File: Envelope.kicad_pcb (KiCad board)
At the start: 2 copper layers, 39.5 x 100 mm, 81 parts, among them J1 Conn_02x05_Odd_Even, J2 Conn_02x03_Odd_Even, J3 Conn_01x06, SW1 SW_SPDT_MSM, SW2 SW_SPDT_MSM, SW3 SW_Push, U1 TL072, U2 ATmega328PB-AU, U3 L7805, Y1 20MHz

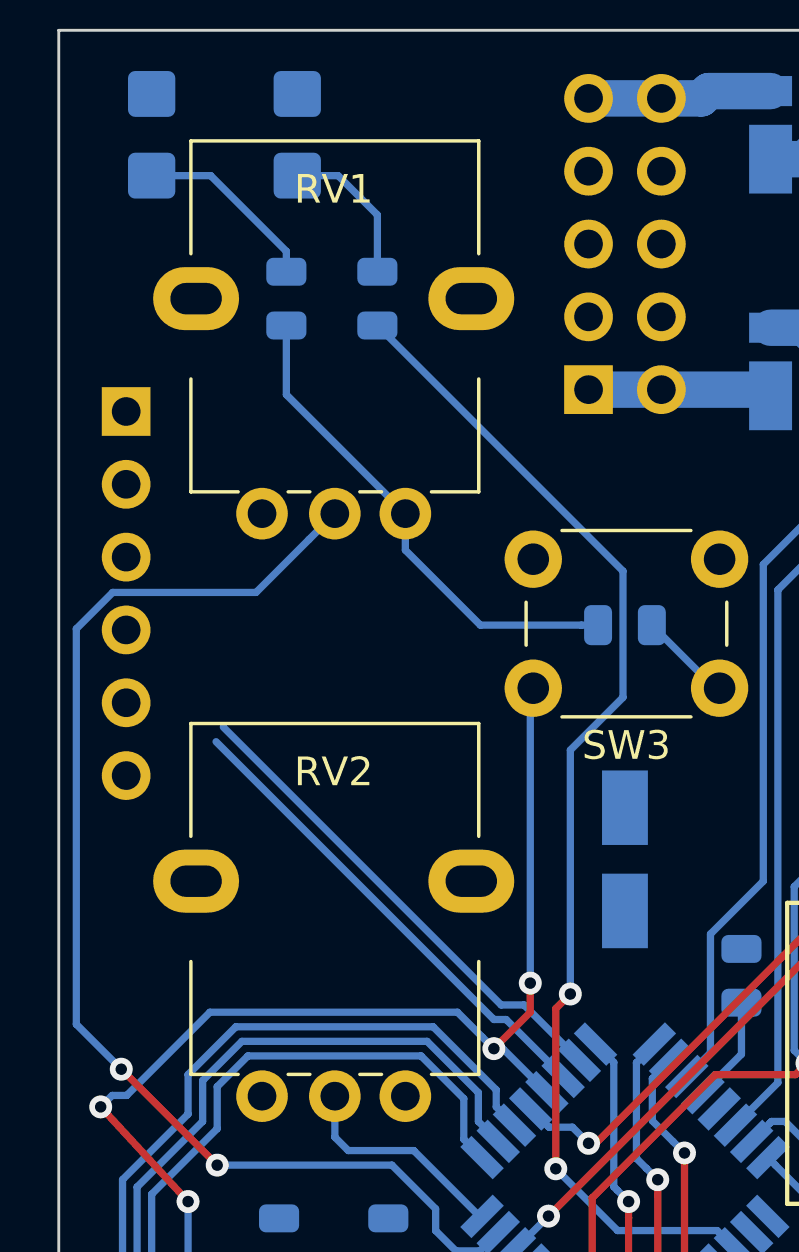
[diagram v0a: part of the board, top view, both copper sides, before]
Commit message: Use 3-pin connector for serial.
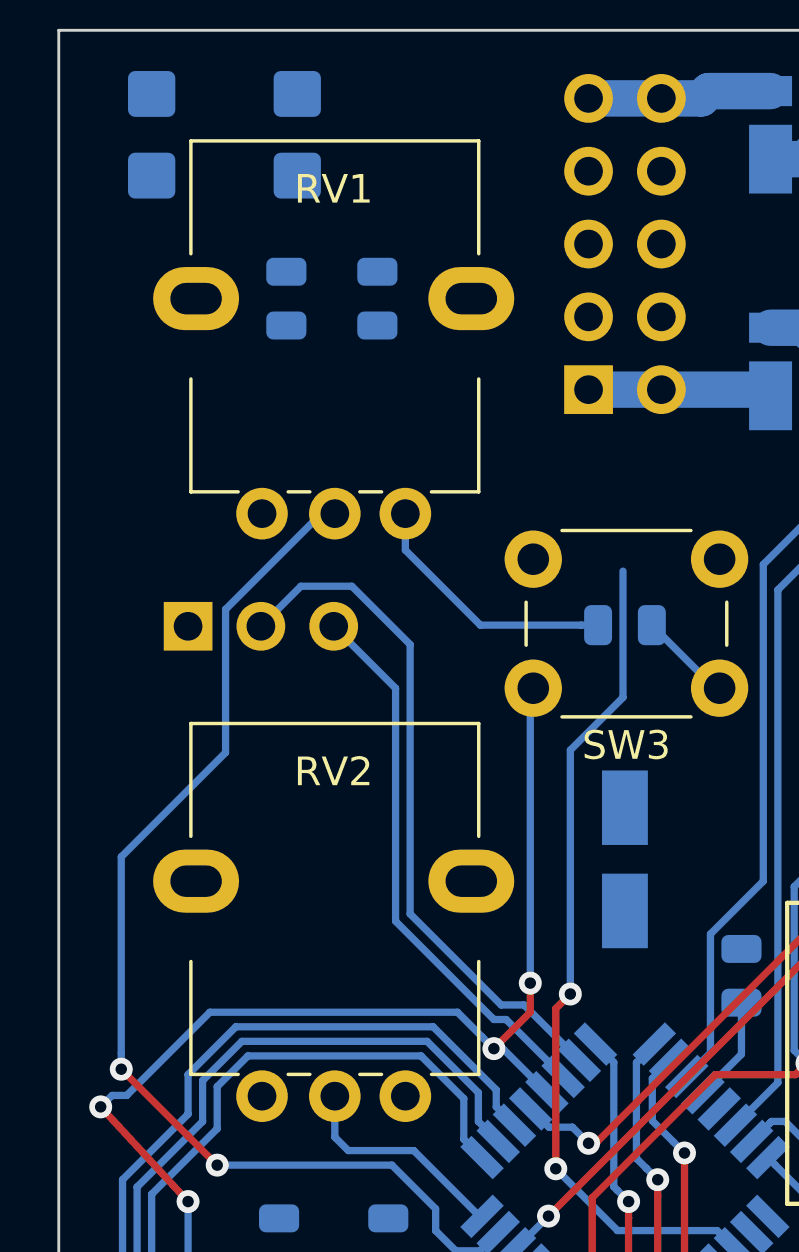
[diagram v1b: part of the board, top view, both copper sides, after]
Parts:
- J3: value Conn_01x06 -> Conn_01x03; footprint Connector_PinHeader_2.54mm:PinHeader_1x06_P2.54mm_Vertical -> Connector_PinHeader_2.54mm:PinHeader_1x03_P2.54mm_Vertical
- moved J3 7.80 mm to (112.0, 68.8), turned to 270 degrees
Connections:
- J3 pad 2: Net-(J3-Pad2) -> /MCU328/TXD/PD1
- J3 pad 3: Net-(J3-Pad3) -> /MCU328/RXD/PD0
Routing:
- net /MCU328/PD7: track 41.4 -> 29.2 mm
- net +5V: track 139.7 -> 131.4 mm
- net /MCU328/TXD/PD1: track 17.2 -> 24.0 mm
- net Net-(D9-Pad2): track 6.51 -> 0.00 mm
- net Net-(D13-Pad2): track 5.34 -> 0.00 mm
- net /MCU328/PC0: track 43.2 -> 39.3 mm
- net /MCU328/RXD/PD0: track 17.3 -> 19.3 mm

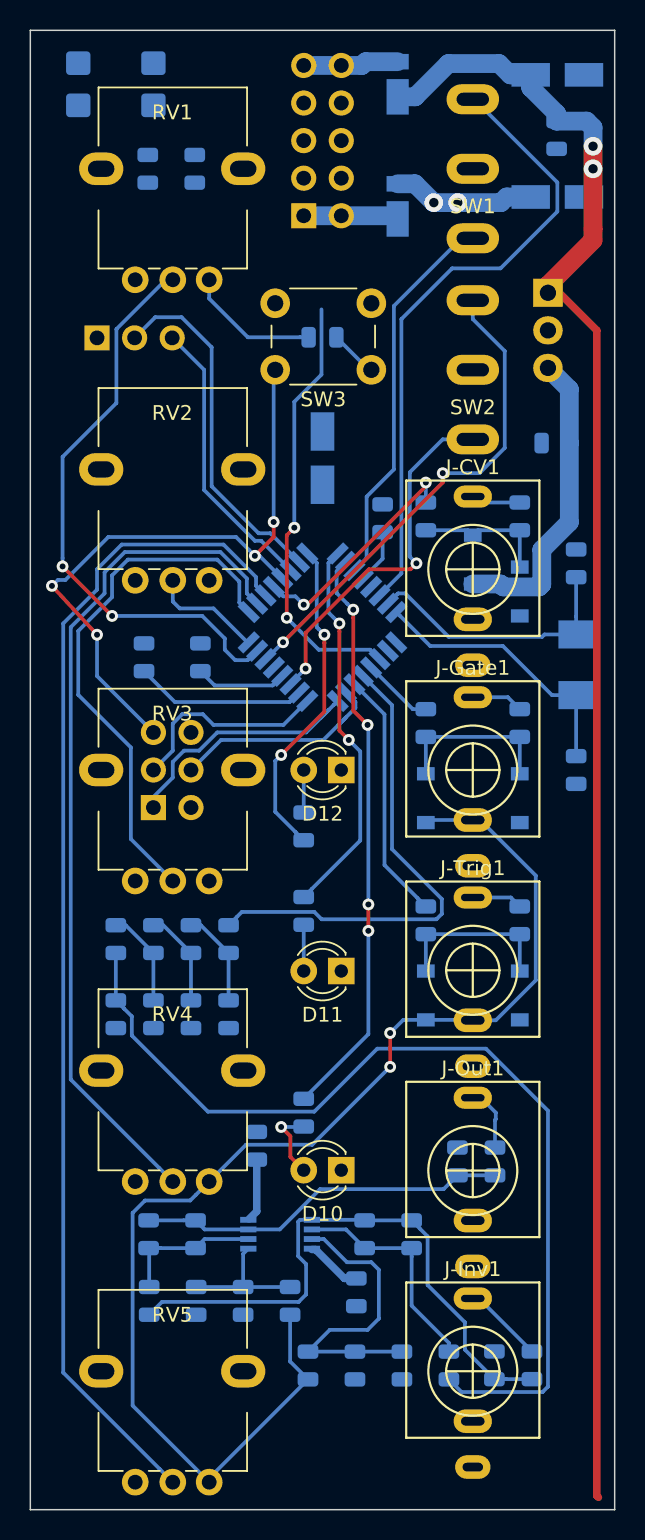
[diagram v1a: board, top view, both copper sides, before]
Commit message: Routed power.
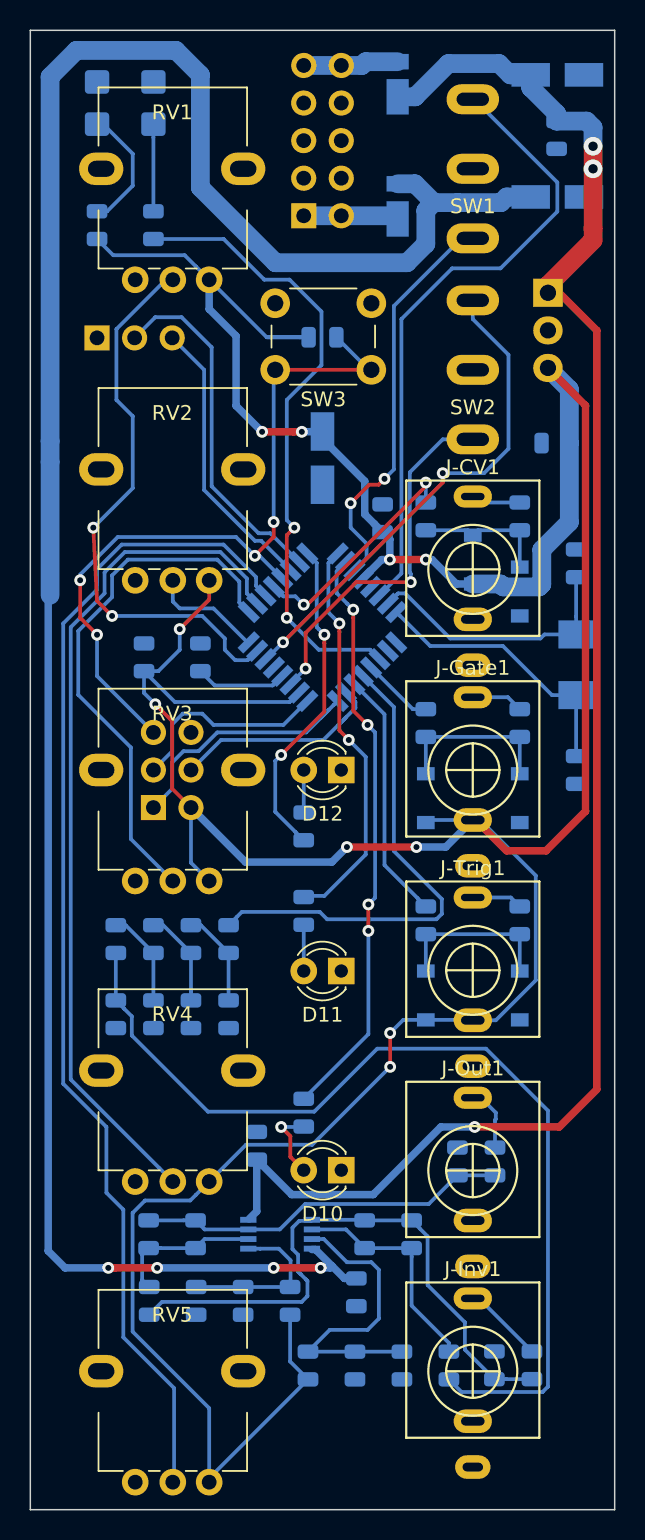
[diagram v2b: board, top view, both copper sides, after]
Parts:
- moved R23 5.13 mm to (112.0, 61.2)
- moved R28 4.72 mm to (115.8, 61.2)
- moved D9 1.80 mm to (112.0, 53.0)
- moved D13 1.27 mm to (115.8, 53.0)
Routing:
- net -12V: track 13.5 -> 152.7 mm, vias 2 -> 4
- net +5V: track 131.4 -> 261.8 mm, vias 2 -> 10
- net /MCU328/PD7: track 29.2 -> 42.9 mm
- net Net-(D9-Pad2): track 0.00 -> 8.53 mm
- net Net-(D13-Pad2): track 0.00 -> 5.89 mm
- net Net-(J2-Pad5): track 47.2 -> 51.5 mm
- net Net-(C7-Pad1): track 9.09 -> 11.3 mm
- net /MCU328/PE0: track 26.2 -> 27.5 mm, vias 0 -> 2
- net /MCU328/PD3: track 25.6 -> 26.6 mm
- net /MCU328/PC0: track 39.3 -> 38.3 mm
- net +12V: track 116.7 -> 116.0 mm, vias 2 -> 3
- net Net-(C6-Pad1): track 39.6 -> 40.2 mm

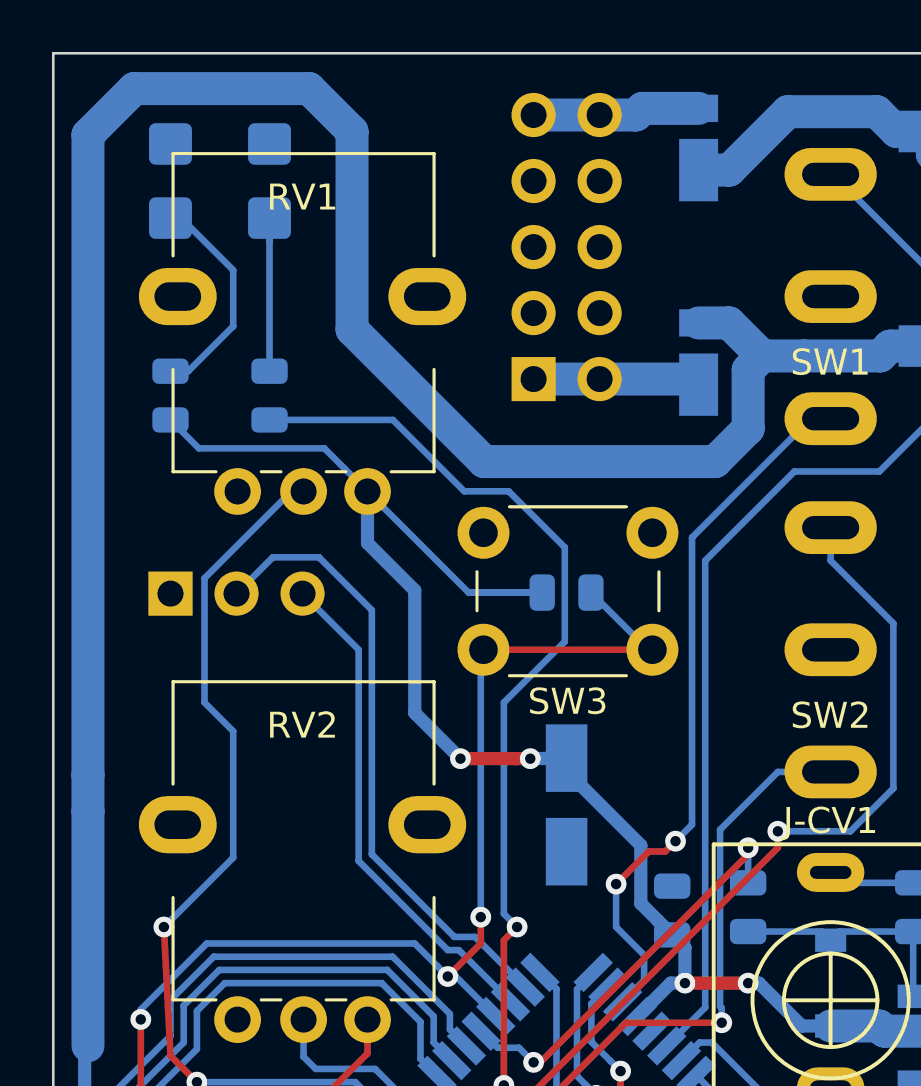
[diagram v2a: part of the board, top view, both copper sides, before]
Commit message: Corrected position of reset button.
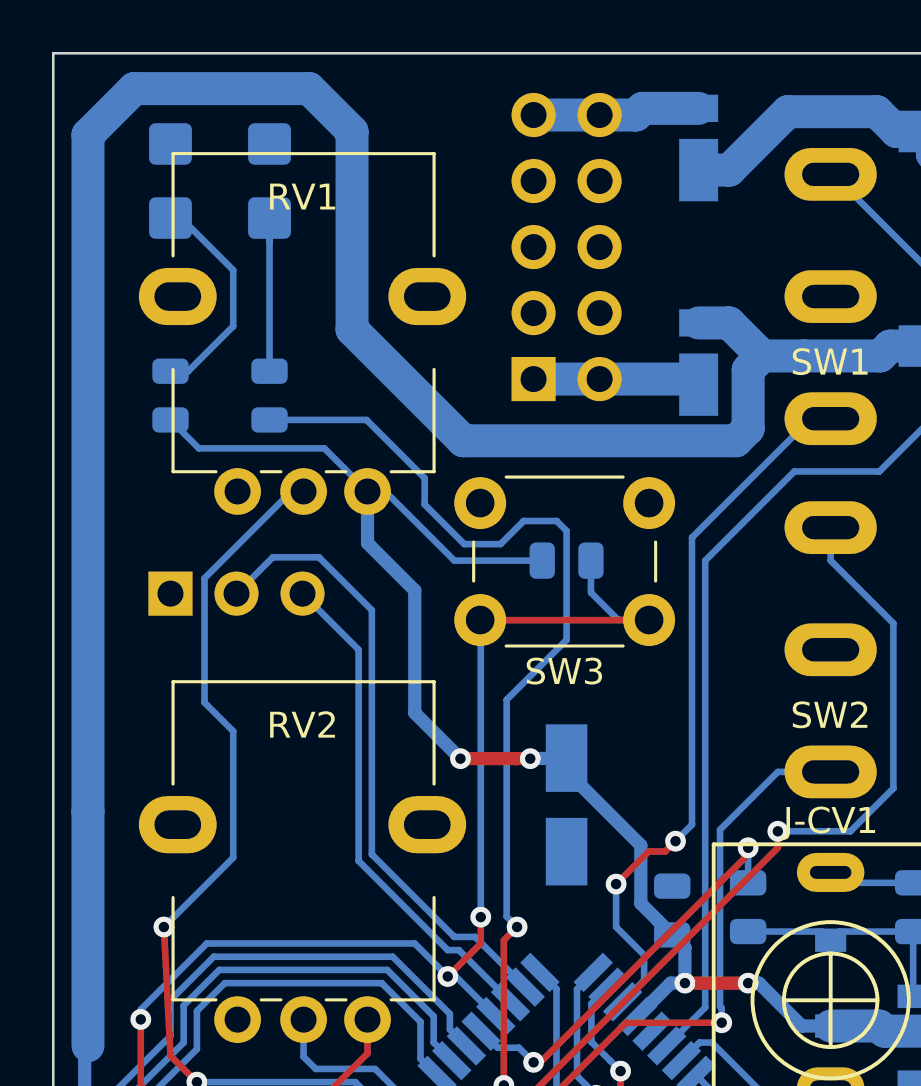
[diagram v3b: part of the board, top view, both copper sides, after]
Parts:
- moved R27 1.23 mm to (127.3, 67.6)
- moved SW3 1.15 mm to (130.4, 69.8)
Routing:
- net +5V: track 261.8 -> 258.6 mm
- net Net-(J2-Pad5): track 51.5 -> 53.4 mm
- net /MCU328/PD7: track 42.9 -> 44.6 mm
- net -12V: track 152.7 -> 152.1 mm

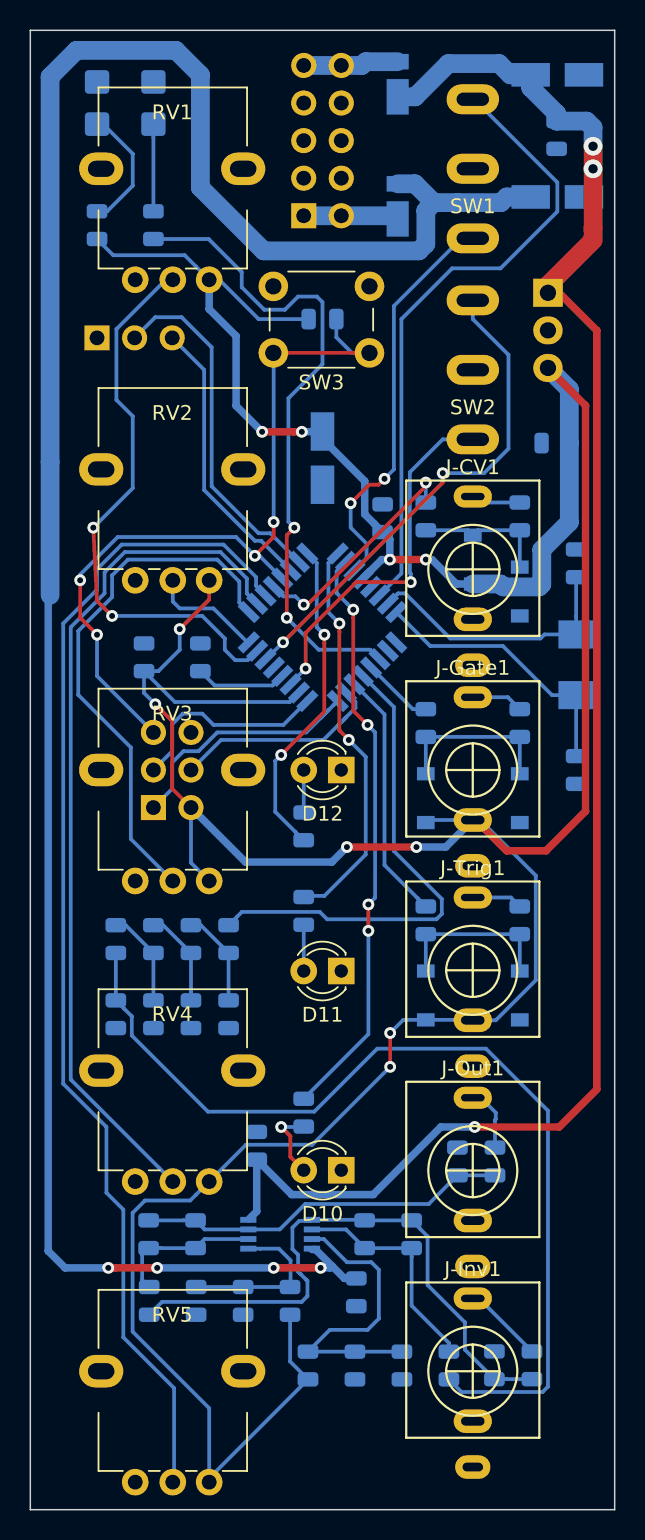
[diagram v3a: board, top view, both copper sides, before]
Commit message: Completed ground fills.
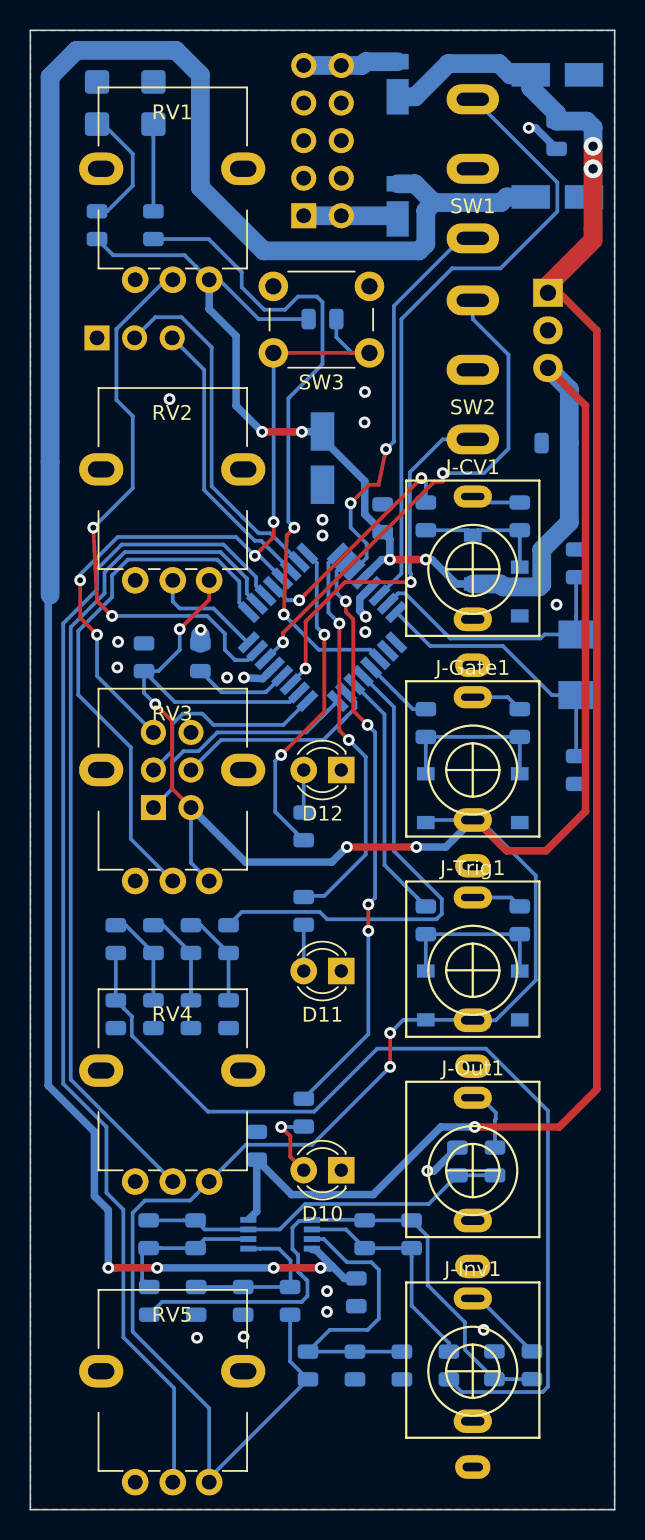
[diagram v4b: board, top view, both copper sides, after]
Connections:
- C1 pad 2: (no net) -> GND
- C10 pad 1: (no net) -> GND
- C11 pad 2: (no net) -> GND
- C12 pad 1: (no net) -> GND
- C13 pad 2: (no net) -> GND
- C14 pad 2: (no net) -> GND
- C15 pad 2: (no net) -> GND
- C16 pad 1: (no net) -> GND
- C17 pad 2: (no net) -> GND
- C18 pad 1: (no net) -> GND
- C19 pad 1: (no net) -> GND
- C2 pad 2: (no net) -> GND
- C20 pad 1: (no net) -> GND
- C3 pad 2: (no net) -> GND
- C4 pad 2: (no net) -> GND
- C5 pad 2: (no net) -> GND
- C7 pad 2: (no net) -> GND
- C9 pad 2: (no net) -> GND
- D10 pad 1: (no net) -> GND
- D11 pad 1: (no net) -> GND
- D12 pad 1: (no net) -> GND
- D13 pad 1: (no net) -> GND
- D2 pad 2: (no net) -> GND
- D4 pad 2: (no net) -> GND
- D6 pad 2: (no net) -> GND
- D9 pad 1: (no net) -> GND
- J-CV1 pad S: (no net) -> GND
- J-Gate1 pad S: (no net) -> GND
- J-Inv1 pad S: (no net) -> GND
- J-Out1 pad S: (no net) -> GND
- J-Trig1 pad S: (no net) -> GND
- J1 pad 3: (no net) -> GND
- J1 pad 4: (no net) -> GND
- J1 pad 5: (no net) -> GND
- J1 pad 6: (no net) -> GND
- J1 pad 7: (no net) -> GND
- J1 pad 8: (no net) -> GND
- J2 pad 6: (no net) -> GND
- J3 pad 1: (no net) -> GND
- R14 pad 1: (no net) -> GND
- R16 pad 2: (no net) -> GND
- R19 pad 1: (no net) -> GND
- R21 pad 2: (no net) -> GND
- RV1 pad 3: (no net) -> GND
- RV2 pad 3: (no net) -> GND
- RV3 pad 3: (no net) -> GND
- RV4 pad 3: (no net) -> GND
- RV5 pad 3: (no net) -> GND
- SW1 pad 2: (no net) -> GND
- SW2 pad 2: (no net) -> GND
- SW3 pad 2: (no net) -> GND
- U2 pad 21: (no net) -> GND
- U2 pad 5: (no net) -> GND
- U3 pad 2: (no net) -> GND
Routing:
- net GND: track 0.00 -> 10.5 mm, vias 0 -> 20
- net -12V: track 152.1 -> 150.3 mm
- added copper zone on B.Cu, net GND
- added copper zone on F.Cu, net GND

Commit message: Silk screens.
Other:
- board text added: "+12"
- board text added: "-12"
- board text added: "AHDSR"
- board text added: "Rev A"
- board text added: "© Marangisto 2018"
